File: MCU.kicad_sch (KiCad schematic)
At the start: 35 parts, among them J1 GT-USB-7010I, J7 USB-5V, SW1 BOOT0, SW6 Reset, U1 STM32F722RETx, U2 AMS1117-3.3, X1 32.768kHz 7pF, Y1 16MHz 10pF

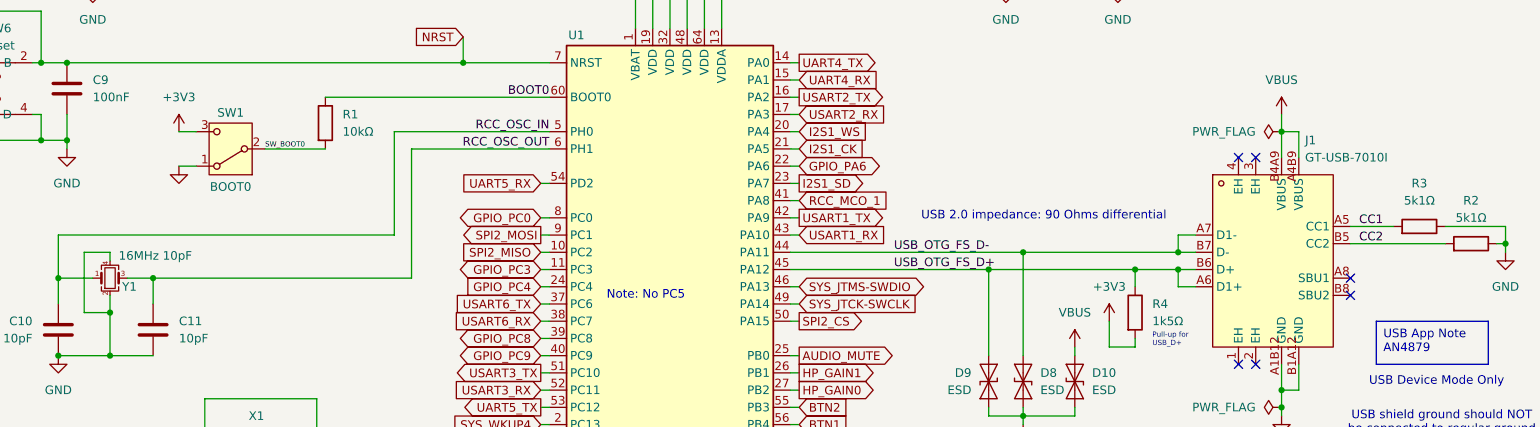
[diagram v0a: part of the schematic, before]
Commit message: Misc cleanups: Consistent part designators, move and clean silkscreen, etc.
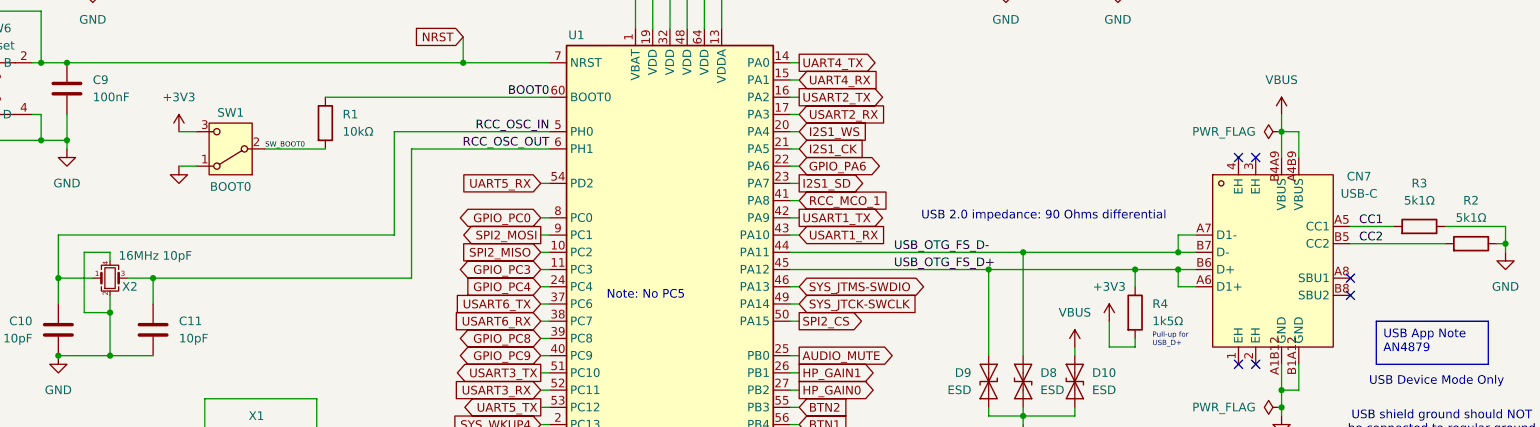
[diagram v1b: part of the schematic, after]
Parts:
- CN7: renamed from J1; value GT-USB-7010I -> USB-C
- renumbered Y1 to X2
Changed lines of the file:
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@@
 		(on_board yes)
 		(dnp no)
-		(fields_autoplaced yes)
-		(property "Reference" "J1"
-			(at 229.5241 68.58 0)
-			(effects
-				(font
-					(size 1.27 1.27)
-				)
-				(justify left)
-			)
-		)
-		(property "Value" "GT-USB-7010I"
-			(at 229.5241 71.12 0)
-			(effects
-				(font
-					(size 1.27 1.27)
-				)
-				(justify left)
+		(property "Reference" "CN7"
+			(at 237.49 73.914 0)
+			(effects
+				(font
+					(size 1.27 1.27)
+				)
+			)
+		)
+		(property "Value" "USB-C"
+			(at 237.49 76.454 0)
+			(effects
+				(font
+					(size 1.27 1.27)
+				)
 			)
 		)
@@
 			(project ""
 				(path "/7cd74113-1f92-4dcc-8610-19aa9fc81e5f/fb10b81b-747c-4030-b31b-dec45474bc0e"
-					(reference "J1")
+					(reference "CN7")
 					(unit 1)
 				)
@@
 		(on_board yes)
 		(dnp no)
-		(property "Reference" "Y1"
+		(property "Reference" "X2"
 			(at 55.118 90.17 0)
 			(effects
@@
 			(project "stm-midi-poc1"
 				(path "/7cd74113-1f92-4dcc-8610-19aa9fc81e5f/fb10b81b-747c-4030-b31b-dec45474bc0e"
-					(reference "Y1")
+					(reference "X2")
 					(unit 1)
 				)
